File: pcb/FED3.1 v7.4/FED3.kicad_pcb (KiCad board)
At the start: 4 copper layers, 108 x 50 mm, 90 parts, among them IC1 MC74VHC1GT125DBVT1G, IC2 TB6612FNG, IC4 RTC PCF8523T, J1 Conn_02x03_Odd_Even, Q2 DMP2035U-7, SW1 Sw, SW2 SPST_TACT-KMR2, U1 ATSAMD21G18A, U2 MIC5504-3.3, U3 MCP73831T, X1 ClockXtal, X2 uXtal, X4 microsd, X5 JST-XH-02

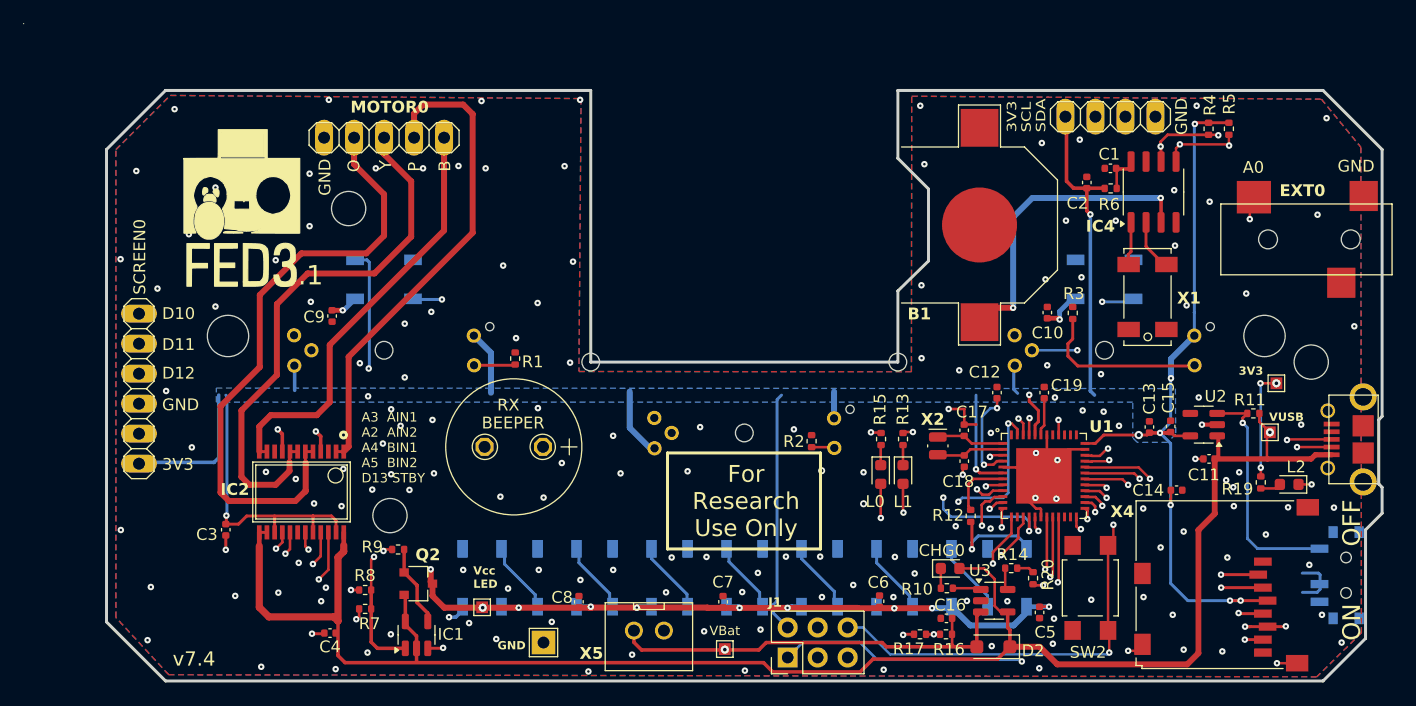
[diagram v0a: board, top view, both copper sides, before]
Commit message: review step 2
Realocação de labels e refªs:
- sem qq alteração no circuito
- alteração na PCB apenas a ver com alocação de Designators/SilkScreen parts
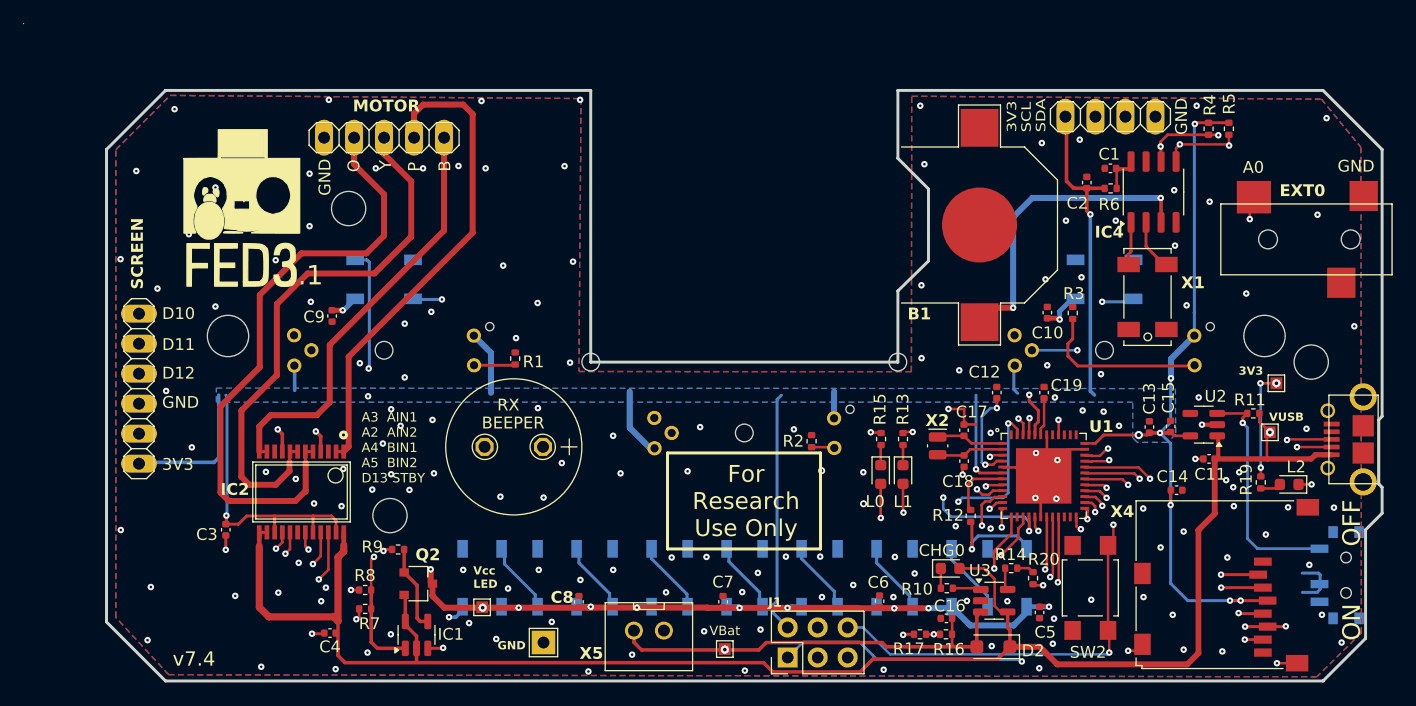
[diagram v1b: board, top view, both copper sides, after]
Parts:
- IC1: value MC74VHC1GT125DBVT1G -> MC74VHC1GT125
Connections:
- net D10 renamed /controler stage/D10
- net D11 renamed /controler stage/D11
- net D12 renamed /controler stage/D12
- net MISO renamed /controler stage/MISO
- net MOSI renamed /controler stage/MOSI
- net SCK renamed /controler stage/SCK
- net SCL renamed /controler stage/SCL
- net SDA renamed /controler stage/SDA
- net SD_CS renamed /controler stage/SD_CS
- net ~{RESET} renamed /controler stage/~{RESET}
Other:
- board text added: "MOTOR"
- board text added: "SCREEN"
